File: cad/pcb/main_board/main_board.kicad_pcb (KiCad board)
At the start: 2 copper layers, 70.5 x 56.5 mm, 76 parts, among them J1 USB_B_Micro, J2 Conn_ARM_JTAG_SWD_10, U1 STM32F401R_B-C_Tx, U2 TLV75533PDRVR, Y1 Crystal_GND23

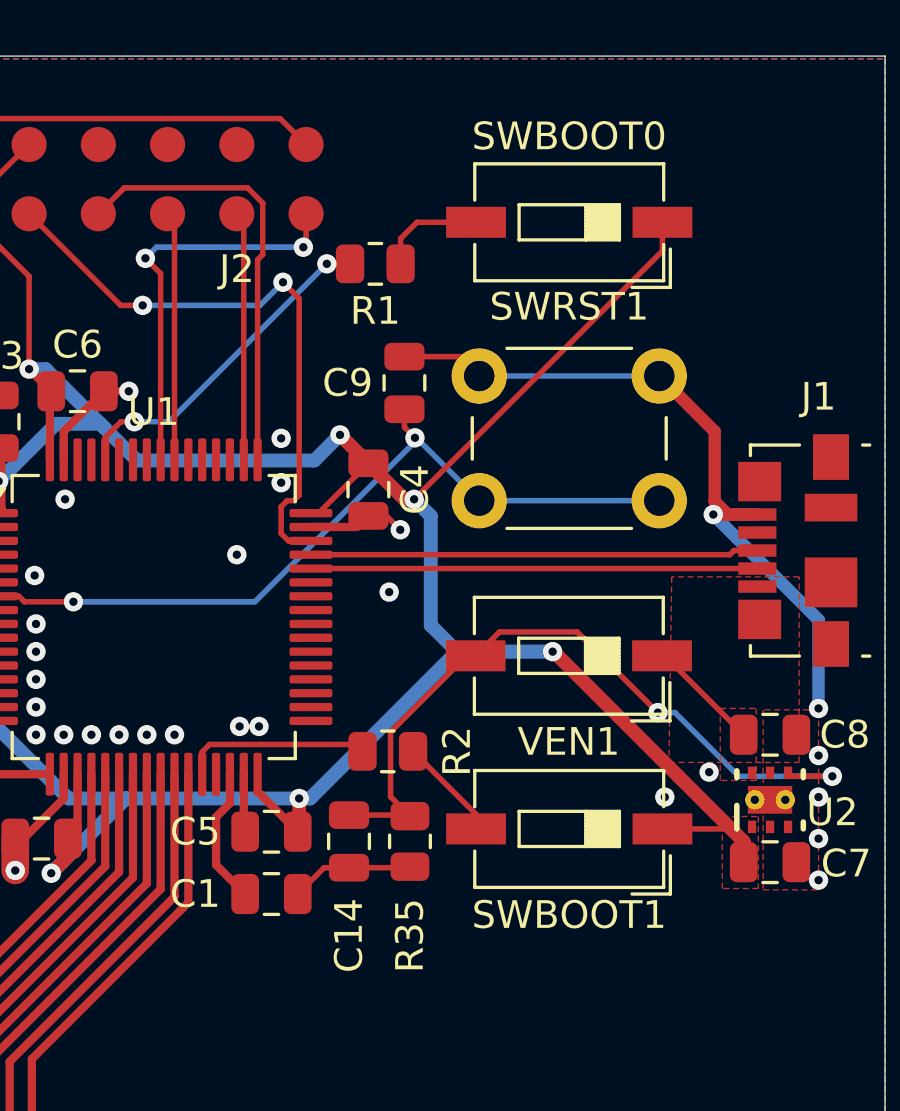
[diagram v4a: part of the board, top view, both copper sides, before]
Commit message: Replace Push button with switch
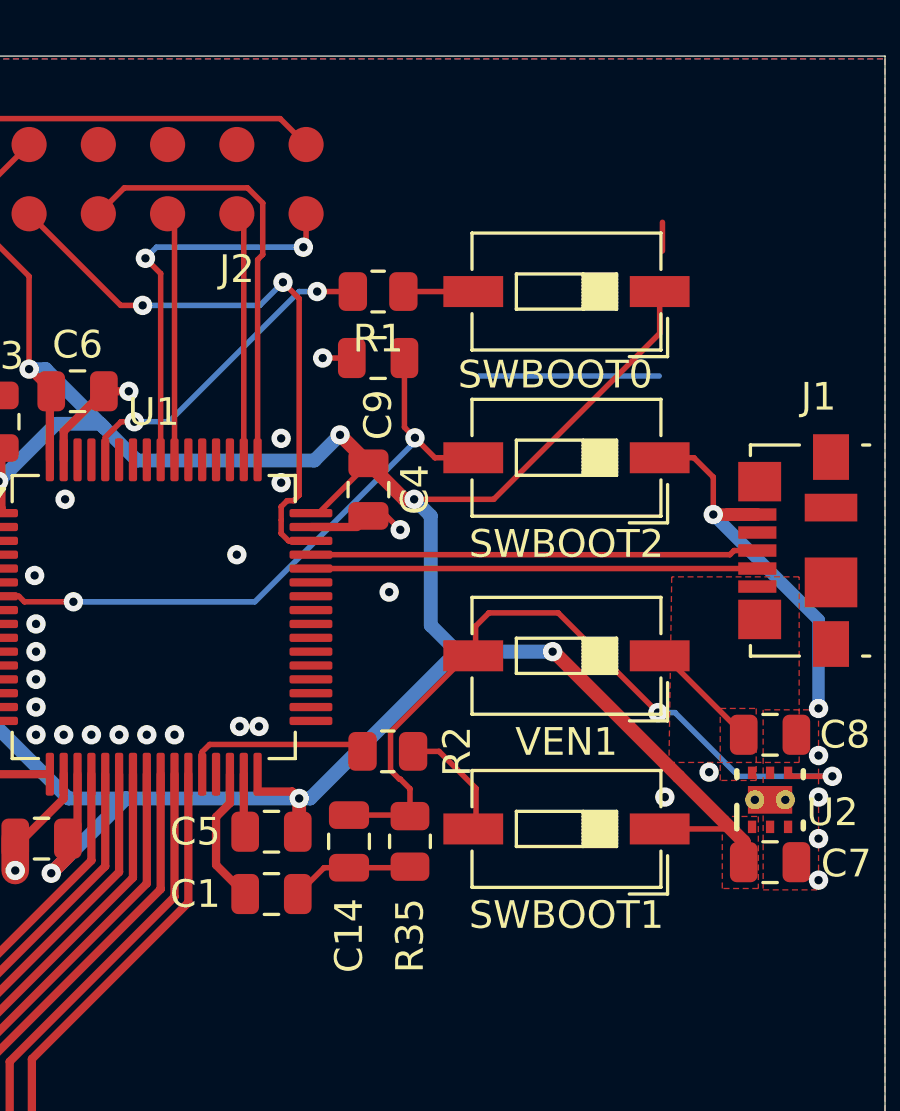
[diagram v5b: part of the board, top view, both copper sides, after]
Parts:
- removed SWRST1: SW_Push, Button_Switch_THT:SW_PUSH_6mm
- added SWBOOT2: SW_DIP_x01, Button_Switch_SMD:SW_DIP_SPSTx01_Slide_6.7x4.1mm_W6.73mm_P2.54mm_LowProfile_JPin, F.Cu at (124.4, 47.0)
- moved SWBOOT0 2.50 mm to (124.4, 41.0)
- moved C9 1.31 mm to (117.6, 43.4), turned to 0 degrees
- moved R1 1.00 mm to (117.6, 41.0)
- moved SWBOOT1 0.10 mm to (124.4, 60.4)
- moved VEN1 0.08 mm to (124.4, 54.1)
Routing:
- net Net-(U1-NRST): track 28.7 -> 23.1 mm
- net VSS: track 102.1 -> 96.8 mm, vias 57 -> 58
- net Net-(R1-Pad1): track 3.88 -> 2.52 mm
- net Net-(U2-EN): track 26.4 -> 27.6 mm
- net VDD: track 120.2 -> 121.1 mm
- net Net-(R2-Pad1): track 3.74 -> 4.29 mm

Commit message: It looks messy
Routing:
- net /MCU/ADC_IN11: track 36.8 -> 37.6 mm
- net /MCU/ADC_IN2: track 35.6 -> 36.3 mm
- net /MCU/ADC_IN1: track 35.0 -> 35.7 mm
- net /MCU/ADC_IN13: track 33.9 -> 34.5 mm

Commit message: Still looks messy
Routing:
- net BOOT0: track 11.9 -> 13.0 mm
- net VSS: vias 58 -> 65
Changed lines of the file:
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@@
+	)
+	(via
+		(at 112.1 42.2)
+		(size 0.7)
+		(drill 0.3)
+		(layers "F.Cu" "B.Cu")
+		(free yes)
+		(net 2)
 	)
 	(via
@@
 	)
 	(via
+		(at 110.9 40.5)
+		(size 0.7)
+		(drill 0.3)
+		(layers "F.Cu" "B.Cu")
+		(free yes)
+		(net 2)
+	)
+	(via
 		(at 133.5 62.25)
 		(size 0.7)
@@
 	)
 	(via
+		(at 112.1 43.7)
+		(size 0.7)
+		(drill 0.3)
+		(layers "F.Cu" "B.Cu")
+		(free yes)
+		(net 2)
+	)
+	(via
 		(at 133.5 60.75)
 		(size 0.7)
@@
 	)
 	(via
+		(at 114 43.6)
+		(size 0.7)
+		(drill 0.3)
+		(layers "F.Cu" "B.Cu")
+		(free yes)
+		(net 2)
+	)
+	(via
 		(at 133.5 59.25)
 		(size 0.7)
@@
 	)
 	(via
+		(at 110.9 43.7)
+		(size 0.7)
+		(drill 0.3)
+		(layers "F.Cu" "B.Cu")
+		(free yes)
+		(net 2)
+	)
+	(via
 		(at 101.9 43.65)
 		(size 0.7)
@@
 	)
 	(via
+		(at 112.1 40.5)
+		(size 0.7)
+		(drill 0.3)
+		(layers "F.Cu" "B.Cu")
+		(free yes)
+		(net 2)
+	)
+	(via
 		(at 97.9 51.75)
 		(size 0.7)
@@
 	(via
 		(at 101.9 49.65)
+		(size 0.7)
+		(drill 0.3)
+		(layers "F.Cu" "B.Cu")
+		(free yes)
+		(net 2)
+	)
+	(via
+		(at 110.9 42.2)
 		(size 0.7)
 		(drill 0.3)
@@
 	)
 	(segment
+		(start 109.1 45.6)
+		(end 108.41759 45.6)
+		(width 0.2)
+		(layer "F.Cu")
+		(net 15)
+	)
+	(segment
+		(start 108.41759 45.6)
+		(end 107.75 46.26759)
+		(width 0.2)
+		(layer "F.Cu")
+		(net 15)
+	)
+	(segment
 		(start 107.75 46.26759)
-		(end 108.31759 45.7)
-		(width 0.2)
-		(layer "F.Cu")
-		(net 15)
-	)
-	(segment
-		(start 108.31759 45.7)
-		(end 108.800008 45.7)
-		(width 0.2)
-		(layer "F.Cu")
-		(net 15)
-	)
-	(segment
-		(start 107.75 47.075)
-		(end 107.75 46.26759)
+		(end 107.75 47.075)
 		(width 0.2)
 		(layer "F.Cu")
@@
 	)
 	(via
-		(at 108.800008 45.7)
+		(at 109.1 45.6)
 		(size 0.7)
 		(drill 0.3)
@@
 	)
 	(segment
-		(start 110.05 45.7)
-		(end 108.800008 45.7)
+		(start 109.25 45.45)
+		(end 109.25 43.55)
 		(width 0.2)
 		(layer "B.Cu")
@@
 	)
 	(segment
-		(start 115.4 41)
-		(end 114.75 41)
+		(start 109.1 45.6)
+		(end 109.25 45.45)
 		(width 0.2)
 		(layer "B.Cu")
@@
 	)
 	(segment
-		(start 114.75 41)
-		(end 110.05 45.7)
-		(width 0.2)
-		(layer "B.Cu")
+		(start 113.5 42.9)
+		(end 115.4 41)
+		(width 0.2)
+		(layer "B.Cu")
+		(net 15)
+	)
+	(segment
+		(start 109.9 42.9)
+		(end 113.5 42.9)
+		(width 0.2)
+		(layer "B.Cu")
+		(net 15)
+	)
+	(segment
+		(start 109.25 43.55)
+		(end 109.9 42.9)
+		(width 0.2)
+		(layer "B.Cu")
